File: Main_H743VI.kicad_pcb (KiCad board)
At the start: 2 copper layers, 200 x 100 mm, 50 parts, among them J1 Conn_01x05, J10 AS7265X, J11 Conn_02x20_Odd_Even, J12 TFTLCD, J2 Conn_01x04, J3 Right Header, J4 Left Header, J5 Screw_Terminal_01x02, J6 DCMI_CAMERA, J7 LCD_CHAR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

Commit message: snapshot
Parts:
- removed J12: TFTLCD, Connector_PinHeader_2.54mm:PinHeader_1x09_P2.54mm_Vertical
- added H1: MountingHole, MountingHole:MountingHole_3.2mm_M3, F.Cu at (55.6, 25.6)
- added H2: MountingHole, MountingHole:MountingHole_3.2mm_M3, F.Cu at (55.9, 114.3)
- added H3: MountingHole, MountingHole:MountingHole_3.2mm_M3, F.Cu at (241.9, 26.7)
- added H4: MountingHole, MountingHole:MountingHole_3.2mm_M3, F.Cu at (241.9, 113.0)
- added J13: UserGPIO, Connector_PinHeader_2.54mm:PinHeader_2x05_P2.54mm_Vertical, F.Cu at (65.4, 49.5)
- added J14: TFT_LCD, Connector_PinHeader_2.54mm:PinHeader_1x14_P2.54mm_Vertical, F.Cu at (233.7, 54.6)
- added R12: 33, Resistor_SMD:R_0603_1608Metric_Pad0.98x0.95mm_HandSolder, F.Cu at (145.0, 32.6)
- added R13: 33, Resistor_SMD:R_0603_1608Metric_Pad0.98x0.95mm_HandSolder, F.Cu at (147.3, 32.6)
- added U2: LM2676S-5, LM2676S-3.3_NOPB:TO127P1435X464-8N, F.Cu at (214.0, 92.7)
- C1, C10, C4, C5, C6, C7, C8, C9: footprint Capacitor_SMD:C_0805_2012Metric_Pad1.18x1.45mm_HandSolder -> Capacitor_SMD:C_0603_1608Metric_Pad1.08x0.95mm_HandSolder
- C2, C3: footprint Capacitor_SMD:C_0805_2012Metric -> Capacitor_SMD:C_0805_2012Metric_Pad1.18x1.45mm_HandSolder
- J1: value Conn_01x05 -> ST-LINK
- J11: value Conn_02x20_Odd_Even -> TFT_LCD2
- J2: value Conn_01x04 -> USB
- R1: footprint Resistor_SMD:R_0805_2012Metric_Pad1.20x1.40mm_HandSolder -> Resistor_SMD:R_0603_1608Metric_Pad0.98x0.95mm_HandSolder
- R2, R3, R4, R5: footprint Resistor_THT:R_Axial_DIN0207_L6.3mm_D2.5mm_P10.16mm_Horizontal -> Resistor_SMD:R_0603_1608Metric_Pad0.98x0.95mm_HandSolder
- U1: value STM32H743VIT6 -> STM32H743VITx
- moved R11 178.9 mm to (203.2, 38.1)
- moved R8 177.0 mm to (203.2, 31.7)
- moved J7 175.2 mm to (205.7, 27.3), turned to 90 degrees
- moved R7 172.2 mm to (203.2, 34.9)
- moved R10 168.3 mm to (179.7, 31.7)
- moved R9 163.1 mm to (179.7, 34.9)
- moved C17 160.8 mm to (228.6, 45.7), turned to 90 degrees
- moved J10 159.4 mm to (182.2, 27.3), turned to 90 degrees
- moved C10 154.3 mm to (151.1, 43.8), turned to -90 degrees
- moved D3 152.5 mm to (200.3, 87.0)
- moved C9 140.7 mm to (127.6, 41.3), turned to -90 degrees
- moved R2 139.6 mm to (131.7, 33.6), turned to 180 degrees
- moved C8 139.2 mm to (139.1, 47.6), turned to 90 degrees
- moved J5 138.8 mm to (206.4, 106.0)
- moved D4 136.6 mm to (175.2, 89.5)
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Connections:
- J11 pad 34: unconnected-(J11-Pin_34-Pad34) -> PB8
- J11 pad 35: unconnected-(J11-Pin_35-Pad35) -> PB9
- J11 pad 36: unconnected-(J11-Pin_36-Pad36) -> PC5
- J11 pad 39: unconnected-(J11-Pin_39-Pad39) -> PB0
- J11 pad 8: /BASEBOARD/TE -> PD2
- J2 pad 2: PA11 -> Net-(J2-Pin_2)
- J2 pad 3: PA10 -> Net-(J2-Pin_3)
- Y1 pad 1: unconnected-(Y1-Tri-State-Pad1) -> +3.3V

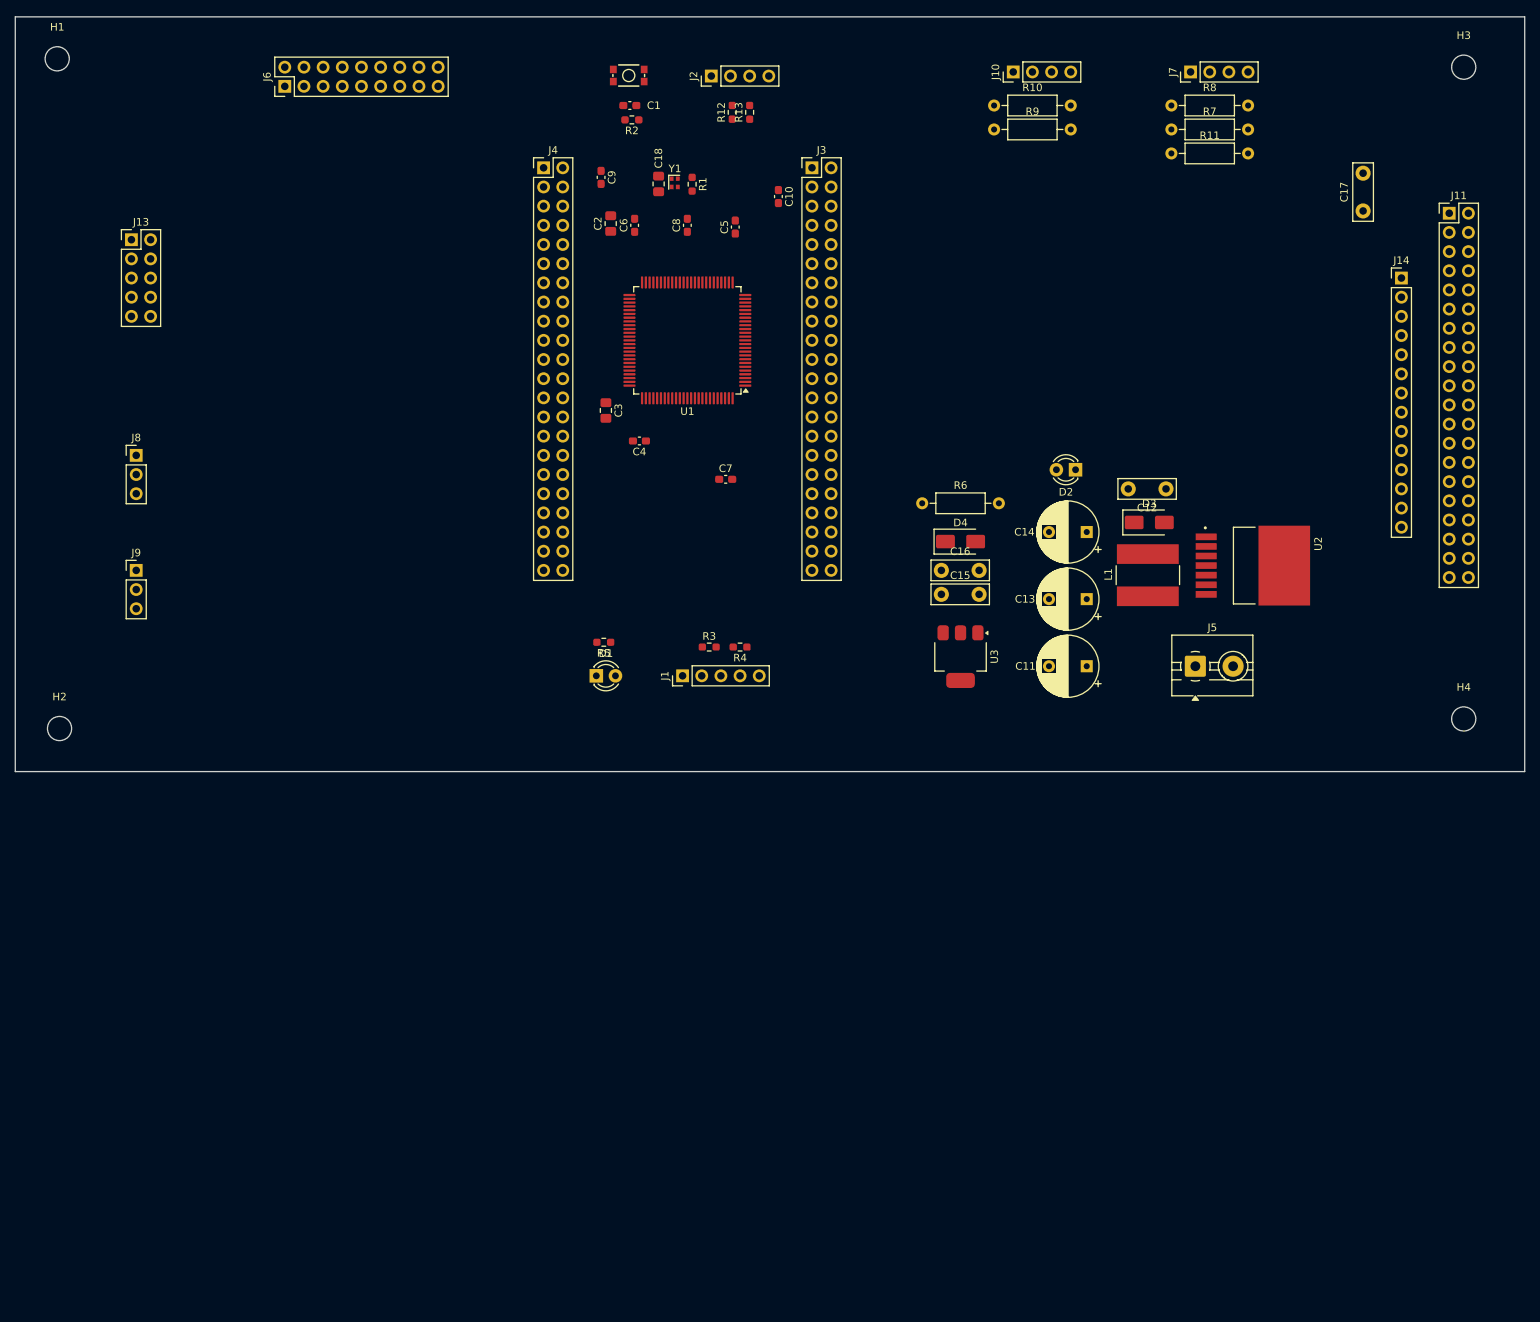
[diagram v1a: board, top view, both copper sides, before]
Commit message: Place all parts and resize board
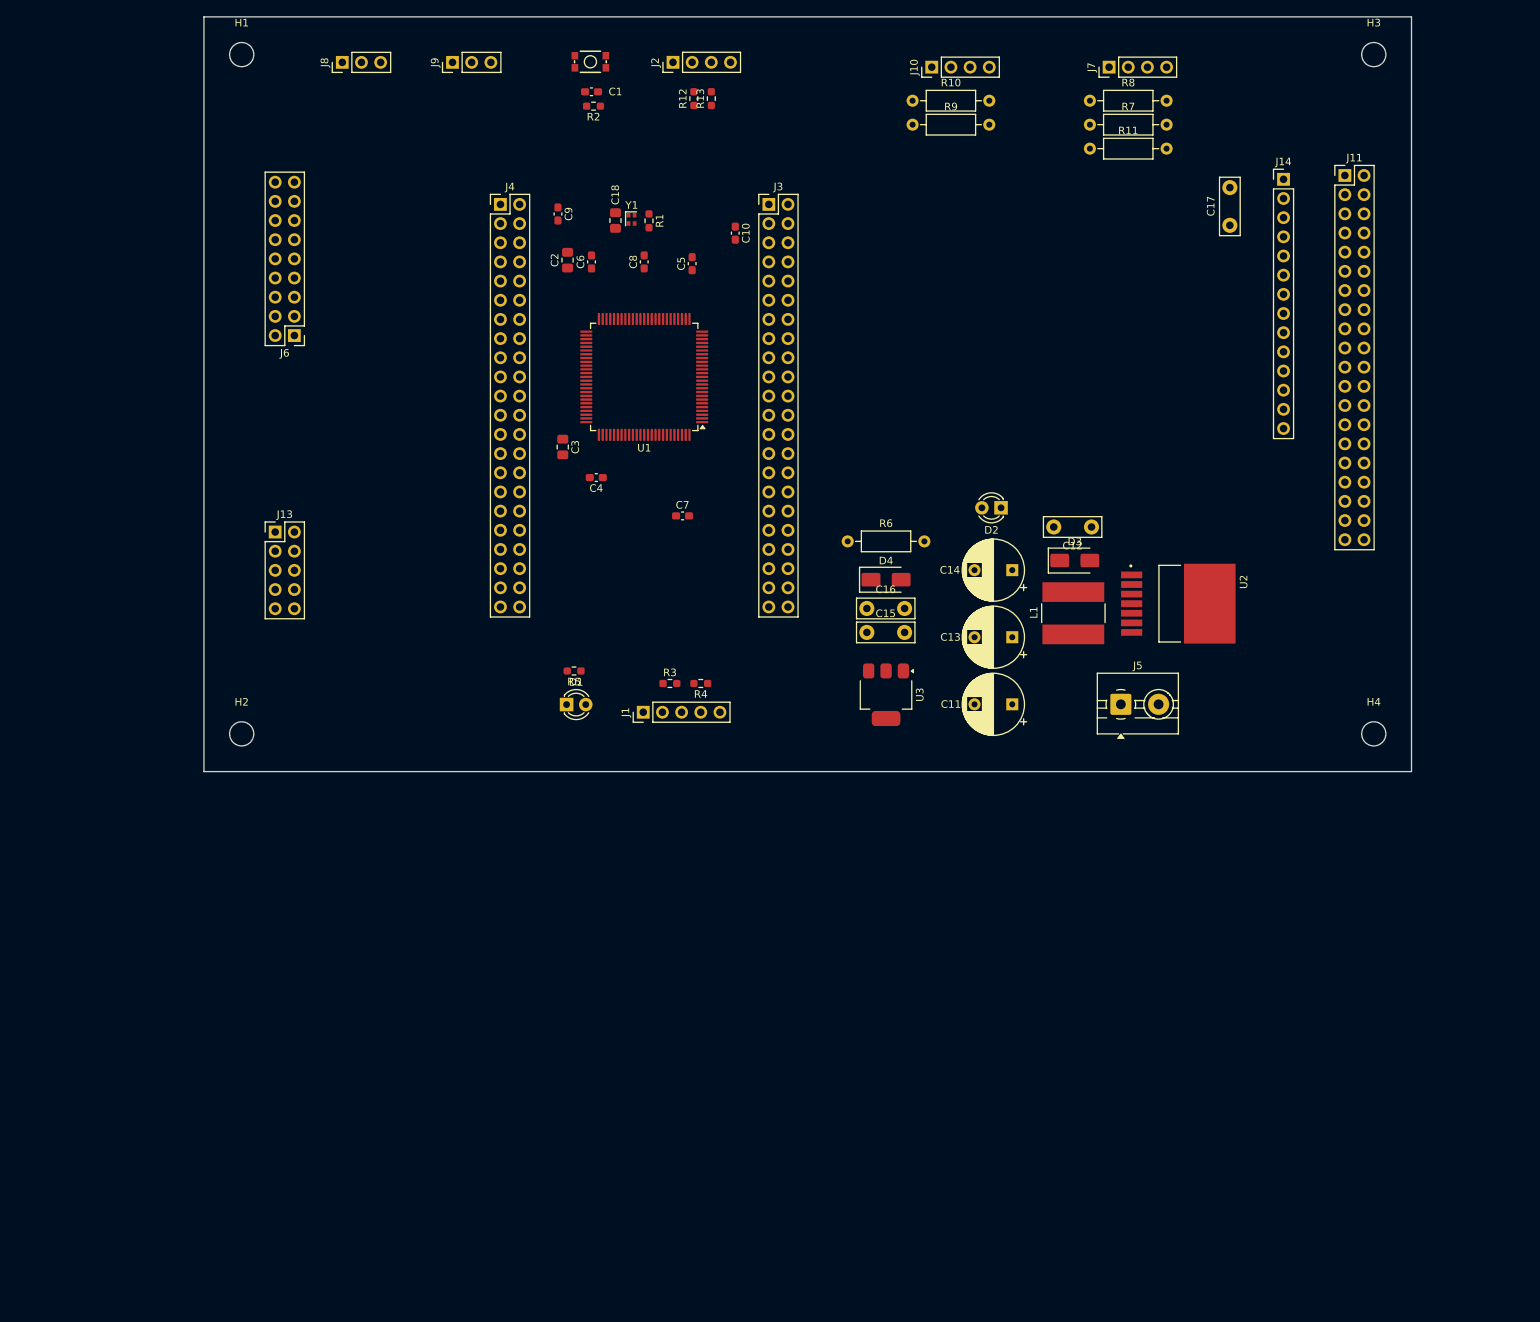
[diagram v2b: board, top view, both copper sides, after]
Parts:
- moved J9 79.3 mm to (107.9, 26.0), turned to 90 degrees
- moved J8 58.8 mm to (93.3, 26.0), turned to 90 degrees
- moved J13 43.2 mm to (84.4, 88.3)
- moved J6 33.0 mm to (87.0, 62.2), turned to 180 degrees
- moved H1 24.5 mm to (80.0, 25.0)
- moved H2 24.1 mm to (80.0, 115.0)
- moved J14 20.4 mm to (218.0, 41.5)
- moved C17 17.8 mm to (210.9, 47.6)
- moved J11 14.7 mm to (226.2, 41.0)
- moved H4 12.1 mm to (230.0, 115.0)
- moved H3 12.0 mm to (230.0, 25.0)
- moved C12 11.1 mm to (192.6, 87.6)
- moved C15 11.1 mm to (162.8, 101.6)
- moved C16 11.1 mm to (162.8, 98.4)
- moved D2 11.1 mm to (180.6, 85.1)
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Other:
- board size 200 x 100 mm -> 160 x 100 mm

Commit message: add servos and fan outputs
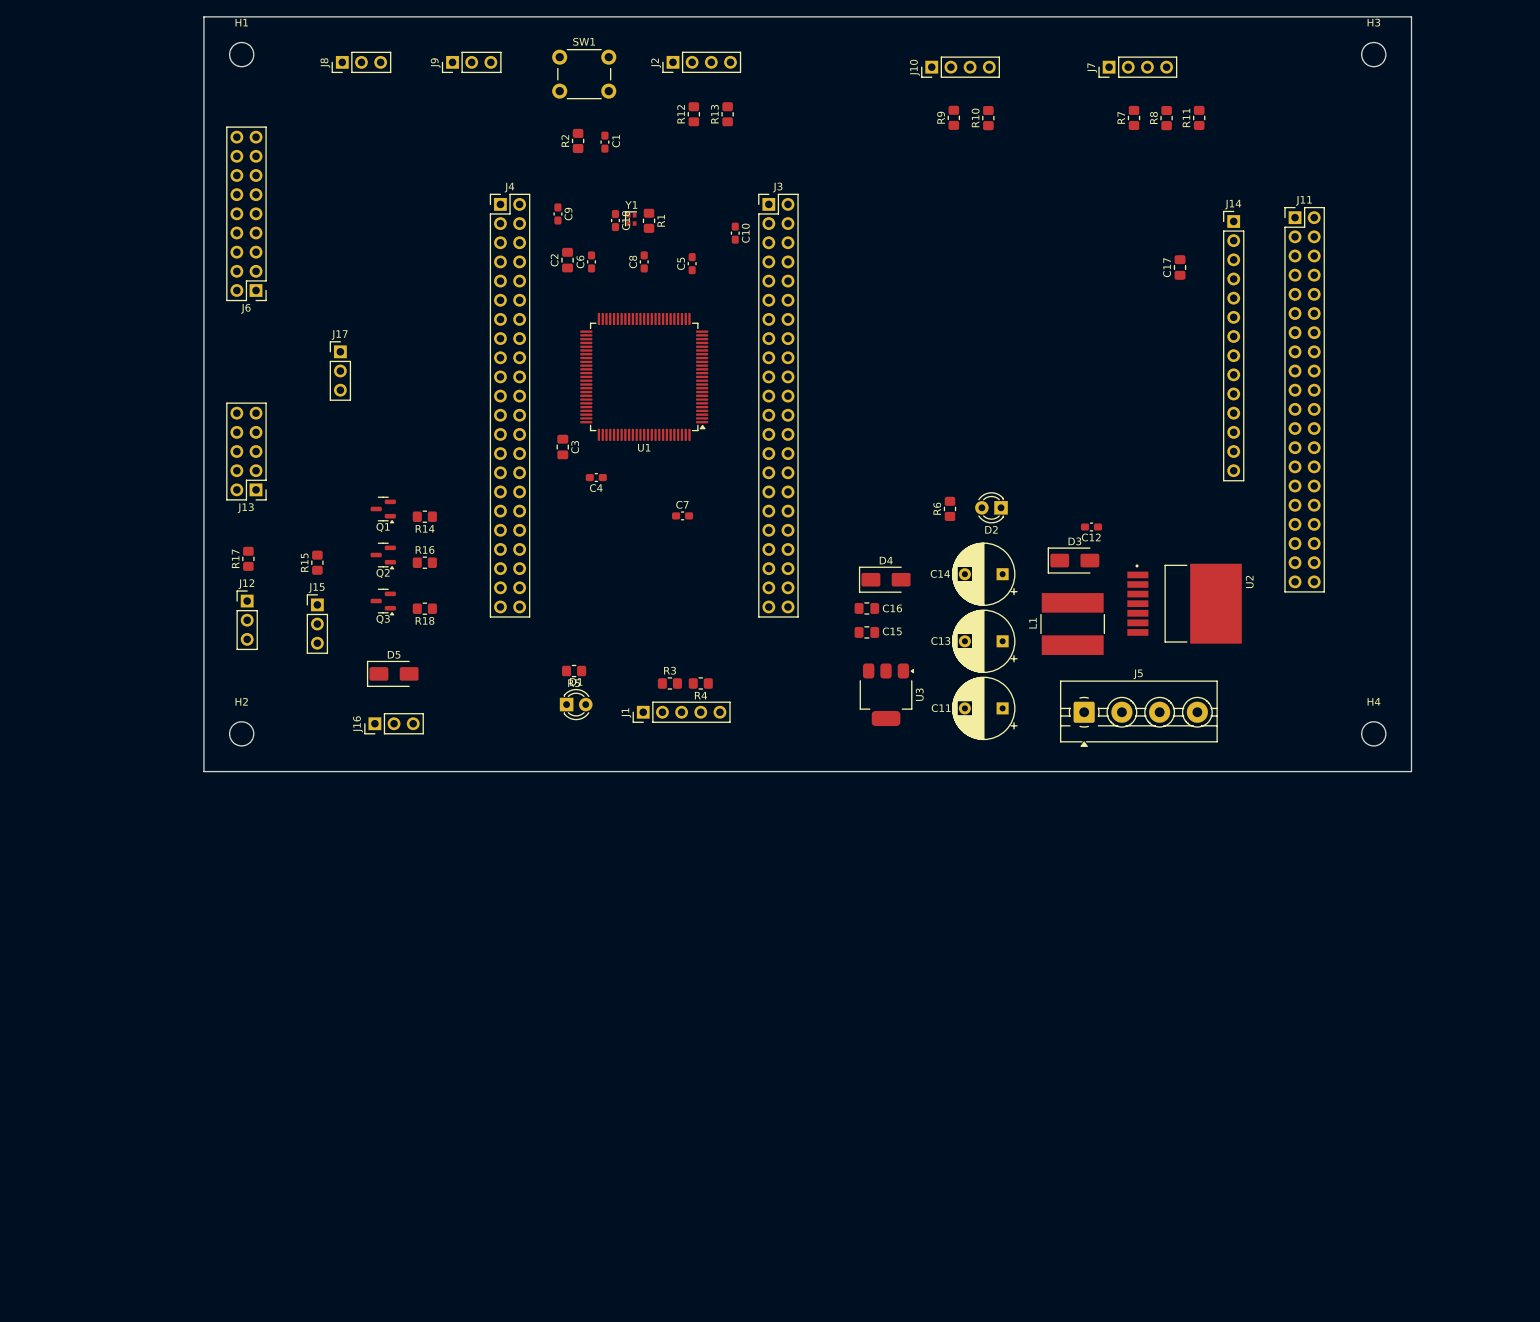
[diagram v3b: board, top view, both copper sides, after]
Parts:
- added D5: SS36, Diode_SMD:D_SMA, F.Cu at (100.2, 107.1)
- added J12: SERVO1, Connector_PinHeader_2.54mm:PinHeader_1x03_P2.54mm_Vertical, F.Cu at (80.7, 97.4)
- added J15: SERVO2, Connector_PinHeader_2.54mm:PinHeader_1x03_P2.54mm_Vertical, F.Cu at (90.0, 97.9)
- added J16: FAN, Connector_PinHeader_2.54mm:PinHeader_1x03_P2.54mm_Vertical, F.Cu at (97.6, 113.7)
- added J17: ADC_IN, Connector_PinHeader_2.54mm:PinHeader_1x03_P2.54mm_Vertical, F.Cu at (93.1, 64.4)
- added Q1: MMBT2222A, Package_TO_SOT_SMD:SOT-23, F.Cu at (98.8, 85.2)
- added Q2: MMBT2222A, Package_TO_SOT_SMD:SOT-23, F.Cu at (98.8, 91.3)
- added Q3: MMBT2222A, Package_TO_SOT_SMD:SOT-23, F.Cu at (98.8, 97.4)
- added R14: 220, Resistor_SMD:R_0805_2012Metric_Pad1.20x1.40mm_HandSolder, F.Cu at (104.3, 86.2)
- added R15: 4.7K, Resistor_SMD:R_0805_2012Metric_Pad1.20x1.40mm_HandSolder, F.Cu at (90.0, 92.3)
- added R16: 220, Resistor_SMD:R_0805_2012Metric_Pad1.20x1.40mm_HandSolder, F.Cu at (104.3, 92.3)
- added R17: 4.7K, Resistor_SMD:R_0805_2012Metric_Pad1.20x1.40mm_HandSolder, F.Cu at (80.9, 91.8)
- added R18: 220, Resistor_SMD:R_0805_2012Metric_Pad1.20x1.40mm_HandSolder, F.Cu at (104.3, 98.4)
- C12: footprint Capacitor_THT:C_Disc_D7.5mm_W2.5mm_P5.00mm -> Capacitor_SMD:C_0603_1608Metric_Pad1.08x0.95mm_HandSolder
- C15, C16, C17: footprint Capacitor_THT:C_Disc_D7.5mm_W2.5mm_P5.00mm -> Capacitor_SMD:C_0805_2012Metric_Pad1.18x1.45mm_HandSolder
- C18: footprint Capacitor_SMD:C_0805_2012Metric_Pad1.18x1.45mm_HandSolder -> Capacitor_SMD:C_0603_1608Metric_Pad1.08x0.95mm_HandSolder
- J13: value UserGPIO -> USER_GPIO
- J5: value Screw_Terminal_01x02 -> Screw_Terminal_01x04; footprint TerminalBlock:TerminalBlock_MaiXu_MX126-5.0-02P_1x02_P5.00mm -> TerminalBlock:TerminalBlock_MaiXu_MX126-5.0-04P_1x04_P5.00mm
- R1, R12, R13, R2, R3, R4, R5: footprint Resistor_SMD:R_0603_1608Metric_Pad0.98x0.95mm_HandSolder -> Resistor_SMD:R_0805_2012Metric_Pad1.20x1.40mm_HandSolder
- R10, R11, R6, R7, R8, R9: footprint Resistor_THT:R_Axial_DIN0207_L6.3mm_D2.5mm_P10.16mm_Horizontal -> Resistor_SMD:R_0805_2012Metric_Pad1.20x1.40mm_HandSolder
- SW1: footprint Button_Switch_THT:Momentary_SMD_4.6x2.8mm -> Button_Switch_THT:SW_PUSH_6mm_H4.3mm
- moved R11 15.0 mm to (206.9, 33.4), turned to 90 degrees
- moved R6 14.2 mm to (173.8, 85.2), turned to 90 degrees
- moved R8 10.4 mm to (202.6, 33.4), turned to 90 degrees
- moved R10 10.3 mm to (178.9, 33.4), turned to 90 degrees
- moved J14 8.65 mm to (211.4, 47.1)
- moved C17 8.65 mm to (204.3, 53.2)
- moved J11 8.65 mm to (219.6, 46.6)
- moved J6 7.84 mm to (81.9, 56.3)
- moved C1 6.90 mm to (128.1, 36.6), turned to 90 degrees
- moved J13 6.14 mm to (81.9, 82.7), turned to 180 degrees
- moved R7 5.91 mm to (198.2, 33.4), turned to 90 degrees
- moved R9 5.54 mm to (174.4, 33.4), turned to 90 degrees
- moved R2 5.05 mm to (124.6, 36.4), turned to 90 degrees
- moved J5 4.97 mm to (191.6, 112.1)
- moved SW1 4.11 mm to (122.1, 25.3)
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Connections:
- C11 pad 1: Net-(J5-Pin_1) -> Net-(J5-Pin_3)
- D1 pad 1: PA1 -> /DEVEBOX/LED
- J11 pad 36: PC5 -> PE3
- J11 pad 7: PC4 -> PC13
- J13 pad 1: GND -> PC0
- J13 pad 2: PC0 -> GND
- J13 pad 3: GND -> PC2
- J13 pad 4: PC2 -> GND
- J13 pad 5: GND -> PC3
- J13 pad 6: PC3 -> GND
- J13 pad 7: GND -> PA0
- J13 pad 8: PA0 -> GND
- J14 pad 14: PC5 -> PE3
- J14 pad 4: PC4 -> PC13
- J3 pad 21: PA11 -> unconnected-(J3-Pin_21-Pad21)
- J3 pad 24: PA12 -> unconnected-(J3-Pin_24-Pad24)
- J4 pad 33: PA1 -> unconnected-(J4-Pin_33-Pad33)
- J5 pad 1: Net-(J5-Pin_1) -> VCC
- J6 pad 17: PC4 -> PC13
- R11 pad 2: PC4 -> PC13
- R12 pad 1: PA11 -> /DEVEBOX/DM
- R13 pad 1: PA12 -> /DEVEBOX/DP
- U1 pad 23: PA1 -> /DEVEBOX/LED
- U1 pad 70: PA11 -> /DEVEBOX/DM
- U1 pad 71: PA12 -> /DEVEBOX/DP
- U2 pad 2: Net-(J5-Pin_1) -> Net-(J5-Pin_3)
